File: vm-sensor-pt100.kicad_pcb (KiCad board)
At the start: 2 copper layers, 36 x 50.5 mm, 27 parts, among them P1 Vi, P2 Vin(+), P3 PT100, P4 ADC, P5 Vo(+), P6 Vo(-), P7 Vin(-), U1 LM2595S-3.3, U2 MCP601T

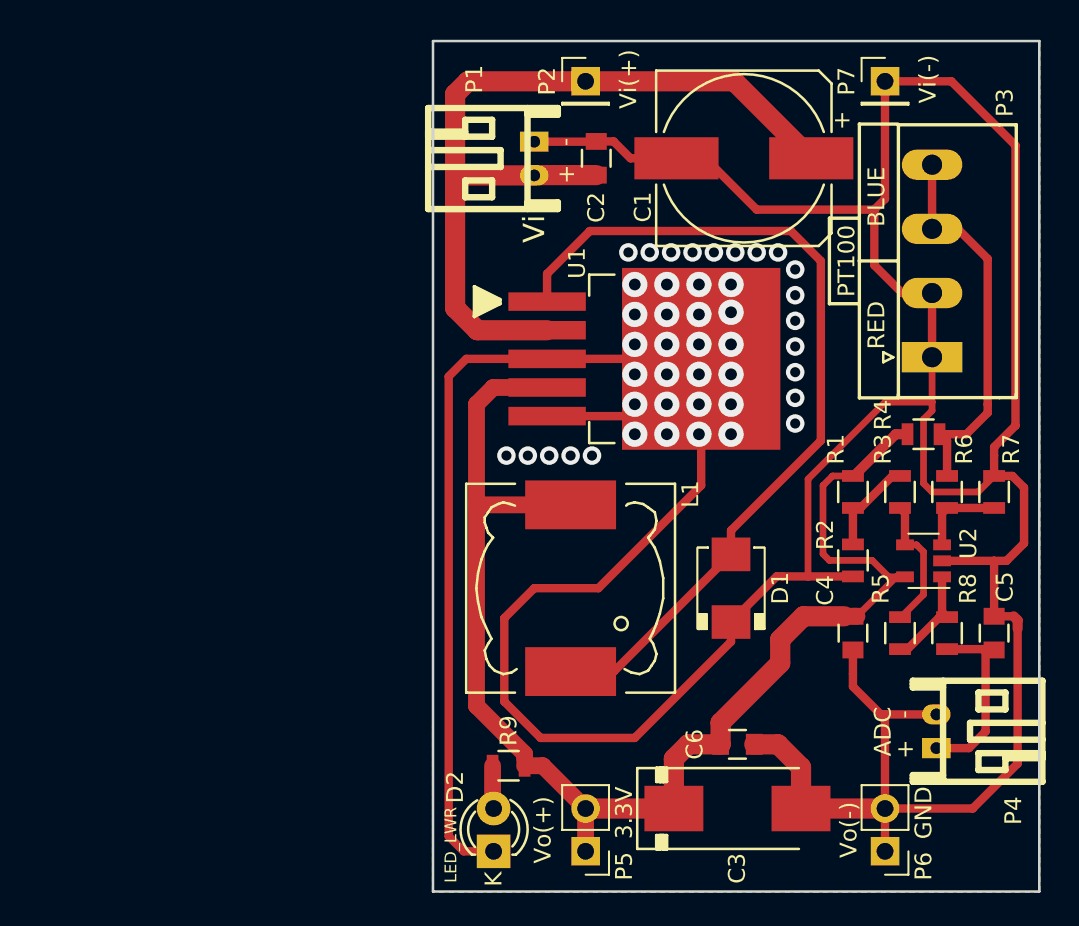
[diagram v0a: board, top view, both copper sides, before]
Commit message: fix BIG MISTAKE-change LM2595S-3.3 to LM2596S-3.3
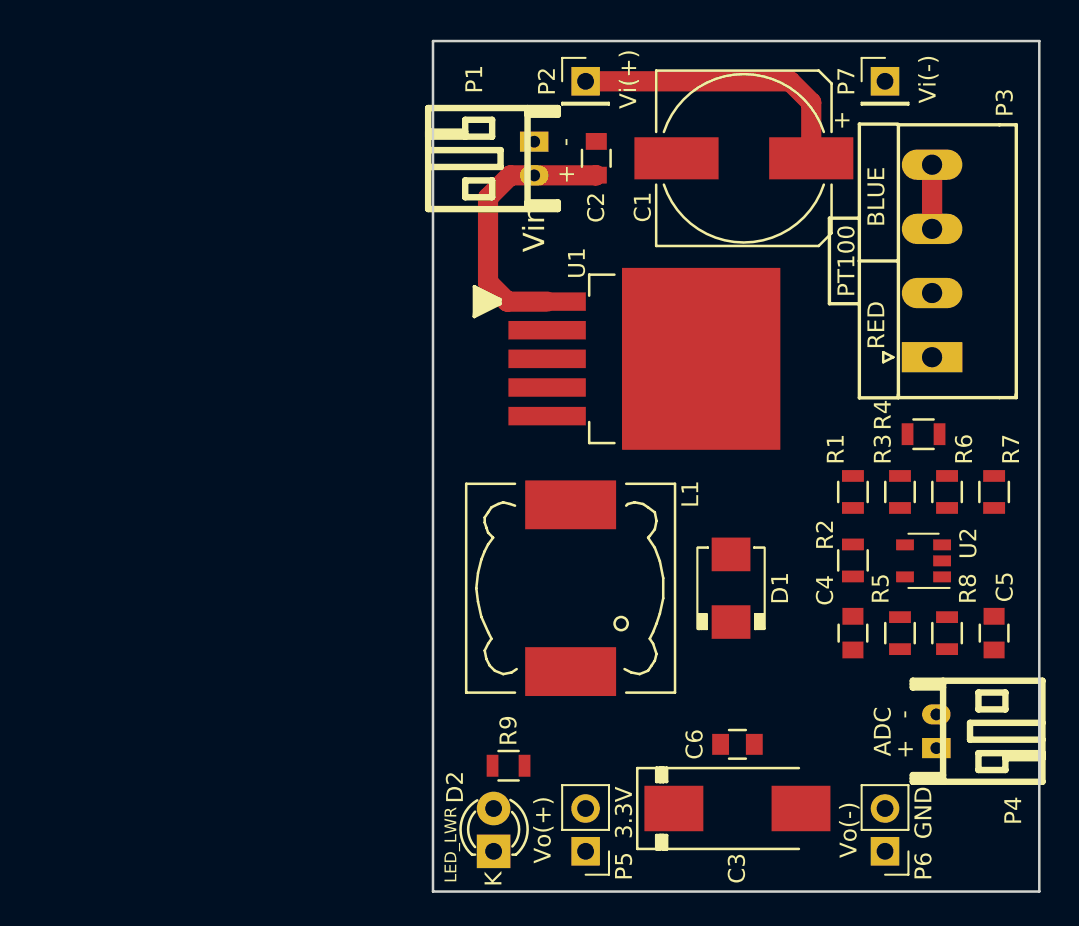
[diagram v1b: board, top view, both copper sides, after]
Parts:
- C2: value 10uF/16v -> 10uF/50v
- D2: value LED_Small -> LED_PWR
- P1: value Vi -> Vin
- U1: value LM2595S-3.3 -> LM2596S-3.3
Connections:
- U1 pad 1: Net-(D1-Pad1) -> VCC
- U1 pad 2: VCC -> Net-(D1-Pad1)
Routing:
- net GND: track 269.0 -> 0.00 mm, vias 24 -> 0
- net +3V3: track 83.3 -> 0.00 mm
- net Net-(D1-Pad1): track 51.7 -> 0.00 mm
- net /Blue: track 23.1 -> 3.81 mm
- net VCC: track 50.5 -> 33.2 mm
- net /ADC: track 11.0 -> 0.00 mm
- net Net-(R3-Pad1): track 8.08 -> 0.00 mm
- net Net-(R5-Pad2): track 6.10 -> 0.00 mm
- net Net-(R1-Pad2): track 5.75 -> 0.00 mm
- net Net-(R6-Pad1): track 5.11 -> 0.00 mm
- net Net-(D2-Pad2): track 2.57 -> 0.00 mm
- net (no net): vias 20 -> 0
- removed copper zone on F.Cu, net GND
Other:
- net class Default: trace_width 0.5 -> 1.2

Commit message: Completed Fix PCB
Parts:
- D1: footprint lib:do214aa-g -> do214aa-g
- moved C1 17.6 mm to (96.5, 89.9), turned to 270 degrees
- moved U1 11.8 mm to (108.2, 85.9), turned to 90 degrees
- moved D1 8.69 mm to (105.9, 94.0), turned to 180 degrees
- moved L1 1.20 mm to (98.6, 103.6), turned to 0 degrees
- moved R9 0.92 mm to (93.7, 112.5)
- moved P3 0.51 mm to (120.1, 88.8)
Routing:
- net GND: track 0.00 -> 226.1 mm, vias 0 -> 24
- net +3V3: track 0.00 -> 73.4 mm
- net Net-(D1-Pad1): track 0.00 -> 27.9 mm
- net /Blue: track 3.81 -> 25.4 mm
- net /ADC: track 0.00 -> 11.0 mm
- net Net-(R3-Pad1): track 0.00 -> 7.93 mm
- net Net-(R5-Pad2): track 0.00 -> 6.10 mm
- net Net-(R1-Pad2): track 0.00 -> 5.75 mm
- net Net-(R6-Pad1): track 0.00 -> 5.11 mm
- net VCC: track 33.2 -> 38.0 mm
- net Net-(D2-Pad2): track 0.00 -> 3.39 mm
- added copper zone on F.Cu, net GND
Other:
- net class Default: trace_width 1.2 -> 1; via_dia 1.1 -> 1.5; via_drill 0.6 -> 0.8
- rule trace_min: 0.254 -> 0.3
- board text removed: "3.3V"
- board text removed: "GND"

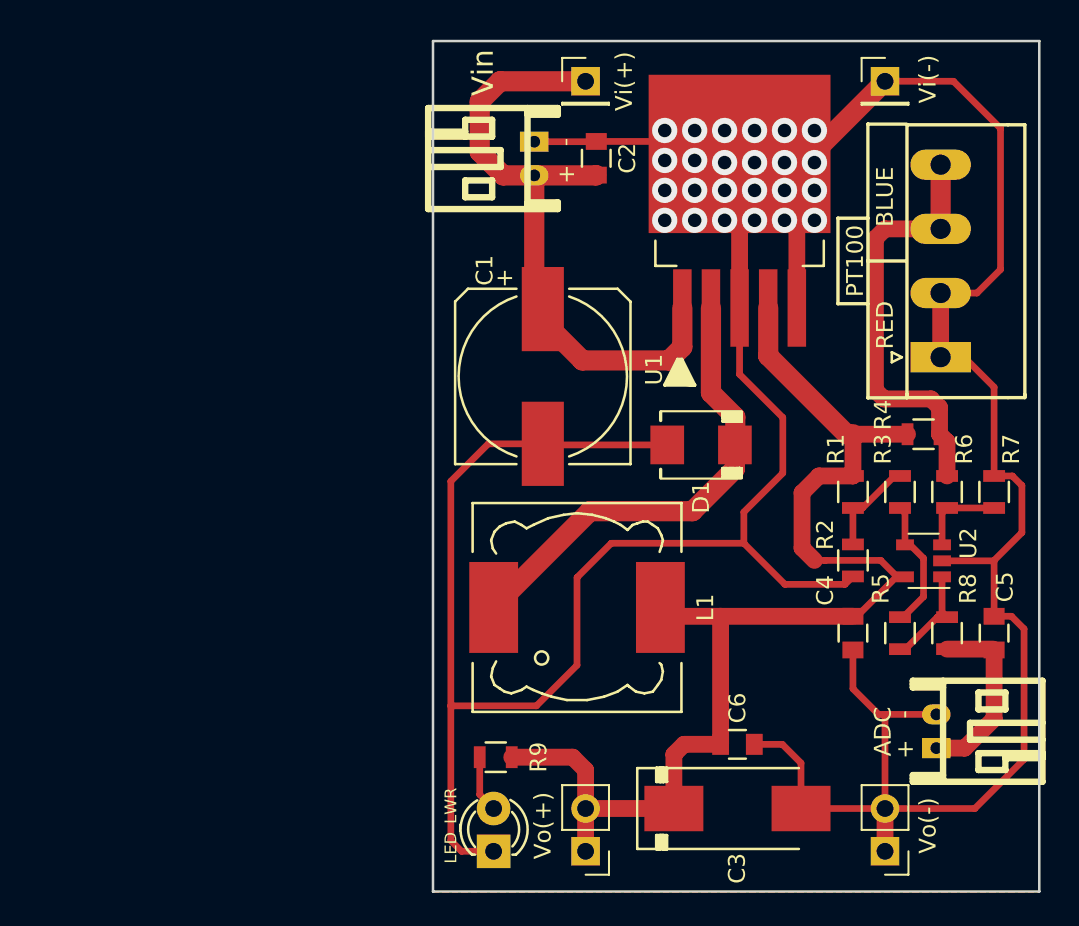
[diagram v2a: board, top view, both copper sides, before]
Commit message: add diode D3-SS34 in Vin & modifu footprint header ADC & PWR
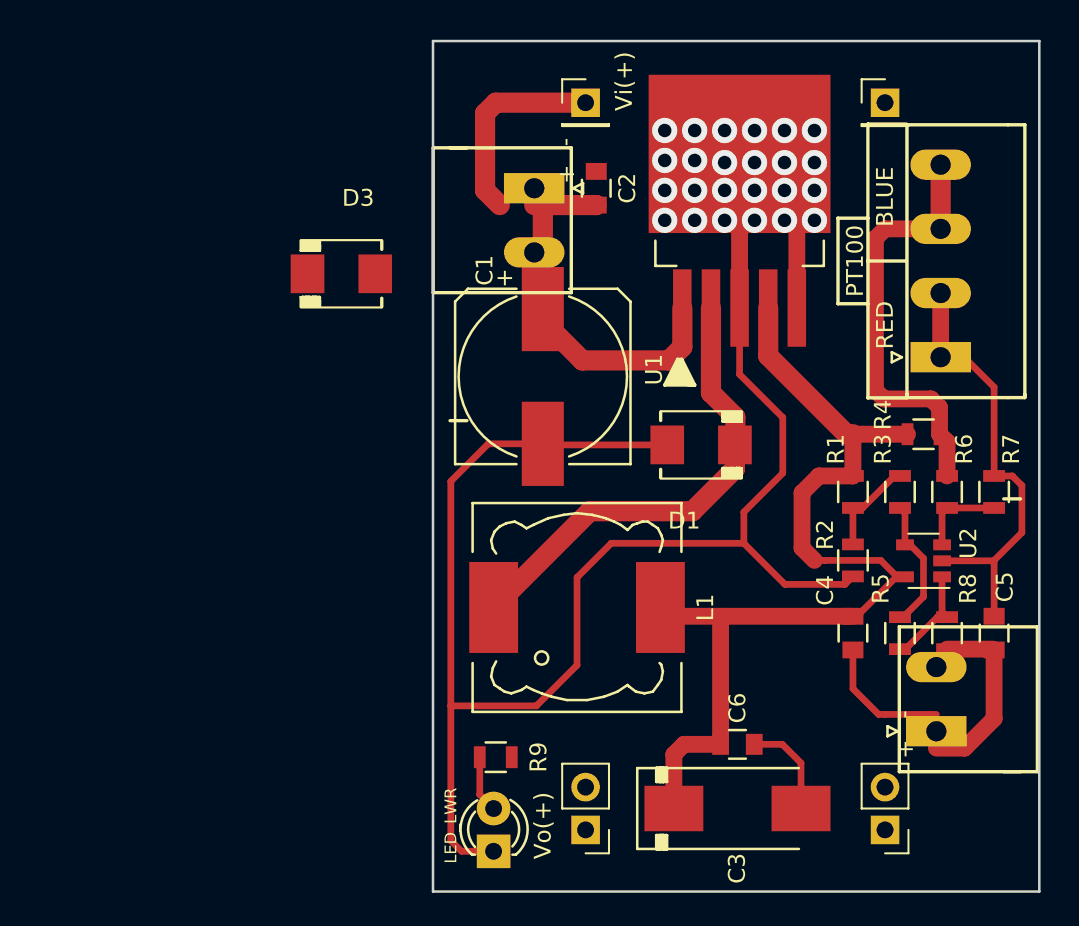
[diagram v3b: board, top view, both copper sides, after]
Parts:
- added D3: SS34, lib:do214aa-g, F.Cu at (84.6, 83.8)
- D1: footprint do214aa-g -> lib:do214aa-g
- P1, P4: footprint lib:s2b-ph-kl -> lib:Pluggable-Terminal-Block-2P-3.81pitch.pretty
- moved C2 1.78 mm to (99.7, 78.7)
- moved P1 1.76 mm to (96.0, 78.7)
- moved P2 1.27 mm to (99.1, 73.7)
- moved P5 1.27 mm to (99.1, 116.8)
- moved P6 1.27 mm to (116.8, 116.8)
- moved P7 1.27 mm to (116.8, 73.7)
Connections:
- C1 pad 1: VCC -> Net-(C1-Pad1)
- C2 pad 1: VCC -> Net-(C1-Pad1)
- U1 pad 1: VCC -> Net-(C1-Pad1)
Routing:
- net GND: track 226.1 -> 155.4 mm
- net VCC: track 38.0 -> 12.0 mm
- net Net-(C1-Pad1): track 0.00 -> 21.3 mm
- net +3V3: track 73.4 -> 58.6 mm
- removed copper zone on F.Cu, net GND
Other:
- net class Default: trace_width 1 -> 1.2
- board text removed: "Vi(-)"
- board text removed: "Vo(-)"

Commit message: fix footprint Pluggable-Terminal-Block-2P-3.81pitch
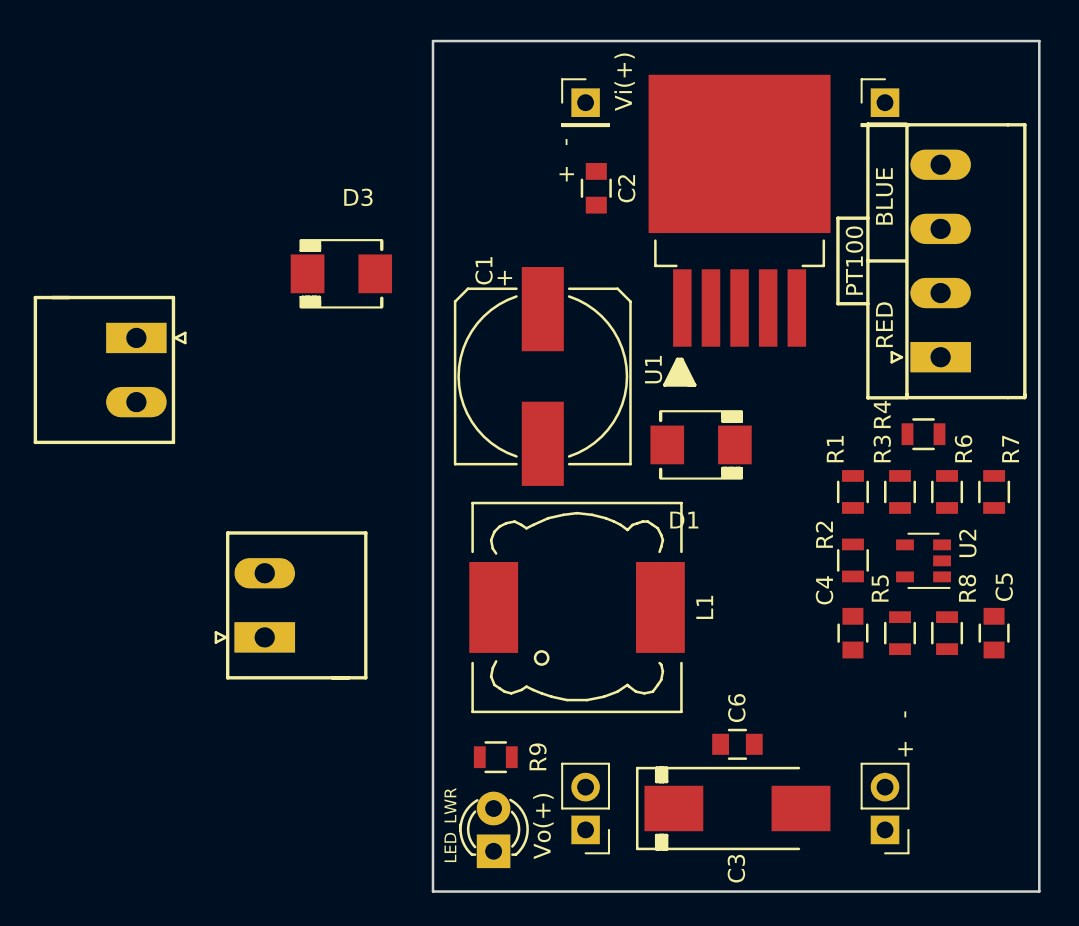
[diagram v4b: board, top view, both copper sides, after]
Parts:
- P1, P4: footprint lib:Pluggable-Terminal-Block-2P-3.81pitch.pretty -> Pluggable-Terminal-Block-2P-3.81pitch.pretty
- moved P4 40.3 mm to (80.0, 105.4)
- moved P1 25.2 mm to (72.4, 87.6)
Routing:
- net GND: track 155.4 -> 0.00 mm, vias 24 -> 0
- net +3V3: track 58.6 -> 0.00 mm
- net Net-(D1-Pad1): track 27.9 -> 0.00 mm
- net /Blue: track 25.4 -> 0.00 mm
- net Net-(C1-Pad1): track 21.3 -> 0.00 mm
- net VCC: track 12.0 -> 0.00 mm
- net /ADC: track 11.0 -> 0.00 mm
- net Net-(R3-Pad1): track 7.93 -> 0.00 mm
- net Net-(R5-Pad2): track 6.10 -> 0.00 mm
- net Net-(R1-Pad2): track 5.75 -> 0.00 mm
- net Net-(R6-Pad1): track 5.11 -> 0.00 mm
- net Net-(D2-Pad2): track 3.39 -> 0.00 mm

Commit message: setup PCB completed
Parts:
- P1: footprint Pluggable-Terminal-Block-2P-3.81pitch.pretty -> lib:Pluggable-Terminal-Block-2P-3.81pitch.pretty
- P4: footprint Pluggable-Terminal-Block-2P-3.81pitch.pretty -> lib:Pluggable-Terminal-Block-2P-3.81pitch.pretty; moved to B.Cu
- moved P4 41.8 mm to (121.5, 110.5), turned to 270 degrees
- moved P1 24.9 mm to (94.5, 76.2)
- moved D3 16.5 mm to (100.5, 79.5), turned to 90 degrees
- moved C2 15.4 mm to (104.8, 93.2), turned to 270 degrees
- moved D1 3.90 mm to (109.8, 93.2)
- moved D2 1.00 mm to (93.6, 117.1)
- moved R9 1.00 mm to (93.7, 111.5)
- moved U1 0.85 mm to (108.5, 86.7)
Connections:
- P1 pad 1: GND -> VCC
- P1 pad 2: VCC -> GND
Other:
- board text removed: "BLUE"
- board text removed: "PT100"
- board text removed: "RED"
